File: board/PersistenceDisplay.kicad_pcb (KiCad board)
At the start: 2 copper layers, 100 x 100 mm, 574 parts, among them J1 Conn_01x01, J2 Conn_01x01, J3 Conn_01x04, J4 Conn_01x04, J5 Conn_01x01, J6 Conn_01x01, J7 Conn_01x02, J8 Conn_01x01, J9 Conn_01x01, Q1 2N7002, Q10 2N7002, Q11 2N7002, Q12 2N7002, Q13 2N7002, Q14 2N7002, Q15 2N7002, Q16 2N7002, Q17 2N7002, Q18 2N7002, Q19 2N7002, Q2 2N7002, Q20 2N7002, Q21 2N7002, Q22 2N7002, Q23 2N7002, Q24 2N7002, Q25 2N7002, Q26 2N7002, Q27 2N7002, Q28 2N7002, Q29 2N7002, Q3 2N7002, Q30 2N7002, Q31 2N7002, Q32 2N7002, Q33 2N7002, Q34 2N7002, Q35 2N7002, Q36 2N7002, Q37 2N7002, Q38 2N7002, Q39 2N7002, Q4 2N7002, Q40 2N7002, Q41 SS8550, Q42 SS8550, Q43 SS8550, Q44 SS8550, Q45 SS8550, Q46 SS8550, Q47 SS8550, Q48 SS8550, Q49 SS8550, Q5 2N7002, Q50 SS8550, Q51 SS8550, Q52 SS8550, Q53 SS8550, Q54 SS8550, Q55 SS8550, Q56 SS8550, Q57 SS8550, Q58 SS8550, Q59 SS8550, Q6 2N7002, Q60 SS8550, Q7 2N7002, Q8 2N7002, Q9 2N7002, U1 AMS1117-3V3, U2 STM32F103VETx, U3 nrf24l01, U4 LM393, Y1 8 MHz, Y2 32.768 kHz, Y3 16 MHz

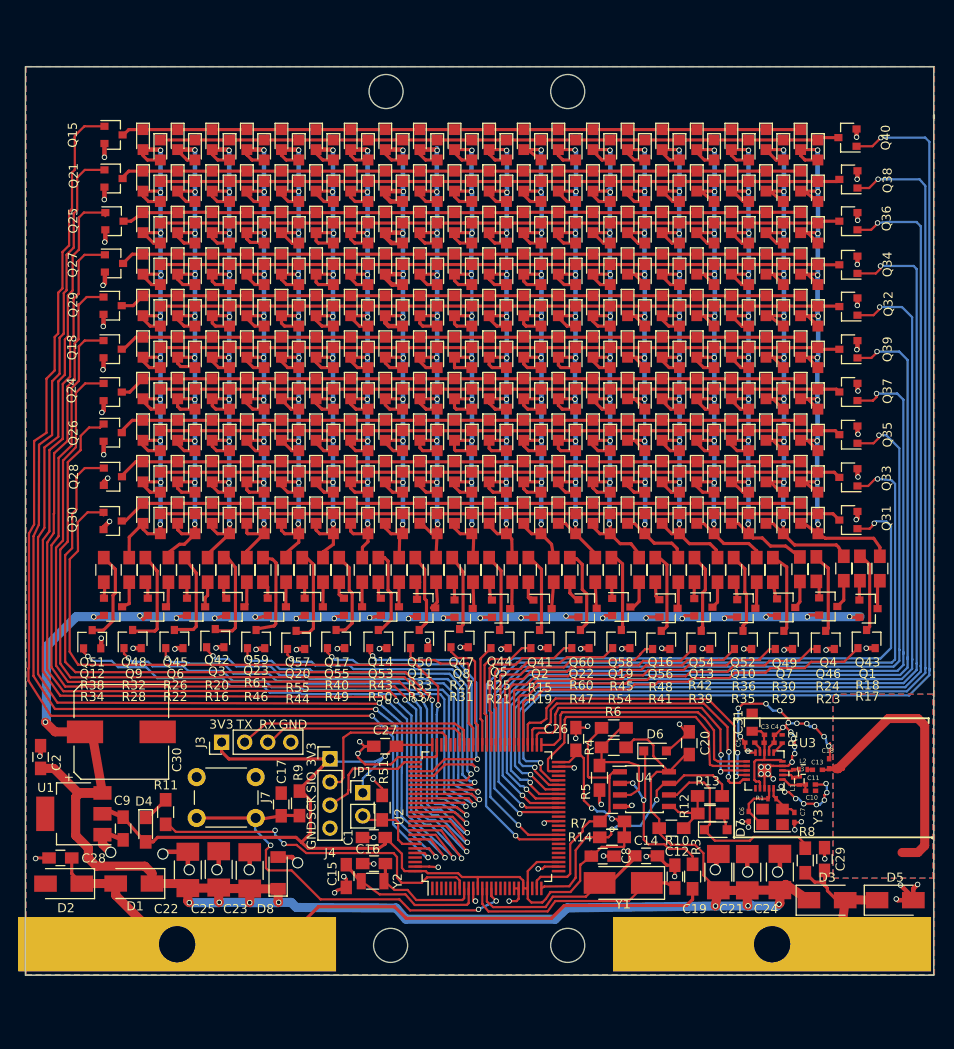
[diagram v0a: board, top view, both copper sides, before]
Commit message: Moved around components and added cutouts
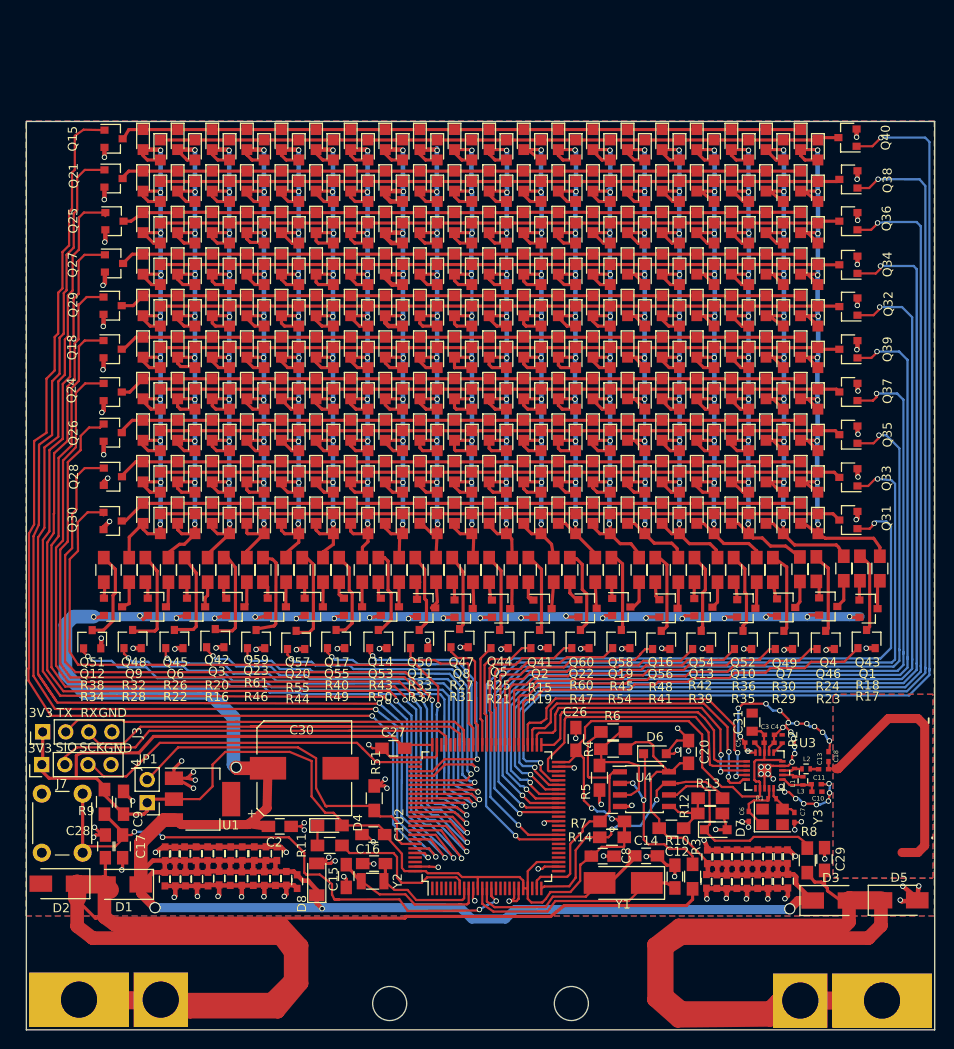
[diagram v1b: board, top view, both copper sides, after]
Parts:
- added C32: 22 uF, Capacitors_SMD:C_0603, F.Cu at (69.1, 136.9)
- added C33: 22 uF, Capacitors_SMD:C_0603, F.Cu at (70.4, 136.9)
- added C34: 22 uF, Capacitors_SMD:C_0603, F.Cu at (72.9, 136.9)
- added C35: 22 uF, Capacitors_SMD:C_0603, F.Cu at (71.6, 136.9)
- added C36: 22 uF, Capacitors_SMD:C_0603, F.Cu at (67.9, 139.7)
- added C37: 22 uF, Capacitors_SMD:C_0603, F.Cu at (71.6, 139.6)
- added C38: 22 uF, Capacitors_SMD:C_0603, F.Cu at (78.0, 136.9)
- added C39: 22 uF, Capacitors_SMD:C_0603, F.Cu at (72.8, 139.6)
- added C40: 22 uF, Capacitors_SMD:C_0603, F.Cu at (66.8, 139.7)
- added C41: 22 uF, Capacitors_SMD:C_0603, F.Cu at (65.6, 139.7)
- added C42: 22 uF, Capacitors_SMD:C_0603, F.Cu at (69.2, 139.7)
- added C43: 22 uF, Capacitors_SMD:C_0603, F.Cu at (75.4, 139.6)
- added C44: 22 uF, Capacitors_SMD:C_0603, F.Cu at (74.1, 139.6)
- added C45: 22 uF, Capacitors_SMD:C_0603, F.Cu at (70.4, 139.7)
- added C46: 22 uF, Capacitors_SMD:C_0603, F.Cu at (77.8, 139.6)
- added C47: 22 uF, Capacitors_SMD:C_0603, F.Cu at (130.9, 137.2)
- added C48: 22 uF, Capacitors_SMD:C_0603, F.Cu at (128.7, 137.2)
- added C49: 22 uF, Capacitors_SMD:C_0603, F.Cu at (129.8, 137.2)
- added C50: 22 uF, Capacitors_SMD:C_0603, F.Cu at (127.5, 137.2)
- added C51: 22 uF, Capacitors_SMD:C_0603, F.Cu at (79.0, 139.6)
- added C52: 22 uF, Capacitors_SMD:C_0603, F.Cu at (80.2, 140.0)
- added C53: 22 uF, Capacitors_SMD:C_0603, F.Cu at (76.6, 139.6)
- added C54: 22 uF, Capacitors_SMD:C_0603, F.Cu at (126.5, 137.3)
- added C55: 22 uF, Capacitors_SMD:C_0603, F.Cu at (125.4, 137.3)
- added C56: 22 uF, Capacitors_SMD:C_0603, F.Cu at (132.1, 137.2)
- added C57: 22 uF, Capacitors_SMD:C_0603, F.Cu at (134.2, 137.2)
- added C58: 22 uF, Capacitors_SMD:C_0603, F.Cu at (128.6, 140.0)
- added C59: 22 uF, Capacitors_SMD:C_0603, F.Cu at (127.5, 140.0)
- added C60: 22 uF, Capacitors_SMD:C_0603, F.Cu at (129.7, 140.0)
- added C61: 22 uF, Capacitors_SMD:C_0603, F.Cu at (134.2, 139.9)
- added C62: 22 uF, Capacitors_SMD:C_0603, F.Cu at (130.9, 140.0)
- added C63: 22 uF, Capacitors_SMD:C_0603, F.Cu at (132.1, 140.0)
- added C64: 22 uF, Capacitors_SMD:C_0603, F.Cu at (133.1, 137.2)
- added C65: 22 uF, Capacitors_SMD:C_0603, F.Cu at (133.1, 140.0)
- added C66: 22 uF, Capacitors_SMD:C_0603, F.Cu at (126.4, 140.0)
- added C67: 22 uF, Capacitors_SMD:C_0603, F.Cu at (125.3, 140.0)
- added J10: Conn_01x01, PersistenceDisplay:BigSlot, F.Cu at (147.0, 148.0)
- added J11: Conn_01x01, PersistenceDisplay:ContactPad, F.Cu at (56.2, 153.1)
- added J12: Conn_01x01, PersistenceDisplay:ContactPad, F.Cu at (144.6, 153.2)
- added J13: Conn_01x01, PersistenceDisplay:BigSlot, F.Cu at (66.0, 148.0)
- added J14: Conn_01x01, PersistenceDisplay:BigSlot, F.Cu at (72.0, 148.0)
- added J15: Conn_01x01, PersistenceDisplay:BigSlot, F.Cu at (141.0, 148.0)
- added J16: Conn_01x01, PersistenceDisplay:BigSlot, F.Cu at (135.0, 148.0)
- added J17: Conn_01x01, PersistenceDisplay:BigSlot, F.Cu at (129.0, 148.0)
- C19, C21, C22, C23, C24, C25: value 100 uF -> 22 uF; footprint Capacitors_SMD:C_1210_HandSoldering -> Capacitors_SMD:C_0603
- moved J1 110.3 mm to (54.0, 148.0)
- moved J2 99.6 mm to (60.0, 148.0)
- moved C24 56.6 mm to (76.8, 136.9)
- moved C21 54.3 mm to (75.5, 136.9)
- moved C19 52.4 mm to (74.2, 136.9)
- moved J4 31.7 mm to (52.1, 127.1), turned to 90 degrees
- moved C2 27.4 mm to (78.3, 133.9), turned to 180 degrees
- moved JP1 23.8 mm to (63.7, 131.3), turned to 180 degrees
- moved R9 21.5 mm to (59.0, 131.2)
- moved C30 20.5 mm to (81.0, 127.5)
- moved D4 20.3 mm to (83.8, 133.8), turned to 0 degrees
- moved J3 19.7 mm to (52.2, 123.5)
- moved J7 19.2 mm to (56.6, 130.3), turned to 270 degrees
- moved R11 18.4 mm to (83.8, 136.0), turned to 180 degrees
- moved C17 18.1 mm to (61.0, 136.1), turned to 270 degrees
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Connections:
- C3 pad 2: Net-(C3-Pad2) -> +3V3
- C31 pad 2: Net-(C3-Pad2) -> +3V3
- C4 pad 2: Net-(C3-Pad2) -> +3V3
- U3 pad 15: Net-(C3-Pad2) -> +3V3
- U3 pad 18: Net-(C3-Pad2) -> +3V3
- U3 pad 7: Net-(C3-Pad2) -> +3V3
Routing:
- net Net-(C29-Pad2): track 15.7 -> 120.3 mm
- net Net-(C28-Pad2): track 89.0 -> 188.4 mm
- net +5V: track 307.9 -> 377.8 mm, vias 28 -> 24
- net +3V3: track 136.1 -> 200.4 mm, vias 3 -> 2
- net GND: track 179.0 -> 235.0 mm, vias 110 -> 127
- net PA10: track 23.2 -> 54.7 mm
- net Net-(JP1-Pad2): track 8.14 -> 38.8 mm
- net PA13: track 18.8 -> 45.4 mm
- net PA14: track 13.0 -> 39.0 mm
- net PC13: track 38.5 -> 17.3 mm, vias 2 -> 0
- net PA9: track 26.8 -> 46.7 mm
- net NRST: track 47.1 -> 64.3 mm, vias 3 -> 4
- net Net-(C3-Pad2): track 11.3 -> 0.00 mm
- net PB7: track 119.7 -> 123.3 mm
- net Net-(C13-Pad1): track 0.58 -> 1.89 mm
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
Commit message: Moved the brushes to the other side of the board
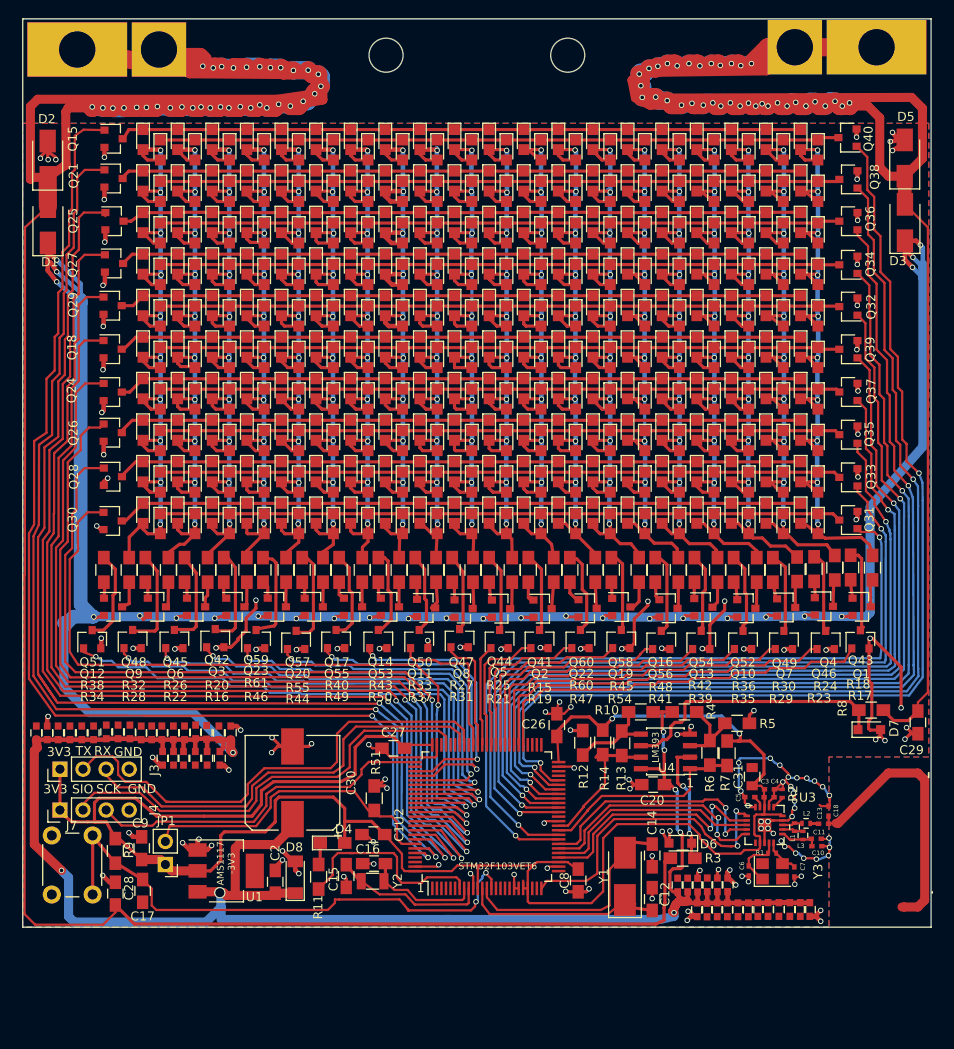
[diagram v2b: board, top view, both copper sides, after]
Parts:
- moved J12 105.0 mm to (144.0, 48.2)
- moved J6 105.0 mm to (135.0, 48.2)
- moved J11 104.6 mm to (56.0, 48.5)
- moved J5 104.6 mm to (65.0, 48.5)
- moved J8 104.4 mm to (110.0, 49.0)
- moved J9 104.4 mm to (90.0, 49.0)
- moved J10 95.8 mm to (146.8, 52.2)
- moved J15 95.8 mm to (140.8, 52.2)
- moved J16 95.8 mm to (134.8, 52.2)
- moved J17 95.8 mm to (128.8, 52.2)
- moved J1 95.5 mm to (53.1, 52.5)
- moved J13 95.5 mm to (65.2, 52.5)
- moved J14 95.5 mm to (71.2, 52.5)
- moved J2 95.5 mm to (59.1, 52.5)
- moved D5 81.7 mm to (147.1, 60.3), turned to 90 degrees
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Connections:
- R13 pad 2: PA2 -> PB1
- R14 pad 1: PA2 -> PB1
- R6 pad 2: PA1 -> PB0
- R7 pad 1: PA1 -> PB0
- U2 pad 24: PA1 -> (no net)
- U2 pad 29: (no net) -> PA4
- U2 pad 30: (no net) -> PA5
- U2 pad 31: (no net) -> PA6
- U2 pad 32: (no net) -> PA7
- U2 pad 35: (no net) -> PB0
- U2 pad 36: (no net) -> PB1
- U2 pad 48: PB11 -> (no net)
- U2 pad 51: PB12 -> (no net)
- U2 pad 52: PB13 -> (no net)
- U2 pad 53: PB14 -> (no net)
- U2 pad 54: PB15 -> (no net)
- U3 pad 1: PB12 -> PA2
- U3 pad 2: PB11 -> PA4
- U3 pad 3: PB13 -> PA5
- U3 pad 4: PB15 -> PA7
- U3 pad 5: PB14 -> PA6
- U4 pad 1: PA1 -> PB0
- U4 pad 7: PA2 -> PB1
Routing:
- net Net-(C28-Pad2): track 188.4 -> 345.2 mm, vias 0 -> 34
- net Net-(C29-Pad2): track 120.3 -> 242.6 mm, vias 0 -> 36
- net +5V: track 377.8 -> 465.8 mm, vias 24 -> 34
- net PB15: track 35.1 -> 0.00 mm, vias 2 -> 0
- net PB14: track 34.6 -> 0.00 mm, vias 2 -> 0
- net PB13: track 32.4 -> 0.00 mm, vias 2 -> 0
- net PB11: track 32.0 -> 0.00 mm
- net PB12: track 29.8 -> 0.00 mm
- net PA1: track 27.5 -> 0.00 mm
- net PA4: track 0.00 -> 27.4 mm, vias 0 -> 2
- net PA7: track 0.00 -> 27.2 mm, vias 0 -> 2
- net PA6: track 0.00 -> 26.7 mm, vias 0 -> 2
- net PA5: track 0.00 -> 24.4 mm
- net PB0: track 0.00 -> 23.1 mm
- net +3V3: track 200.4 -> 221.7 mm
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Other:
- board text added: "1"
- board text added: "AMS1117 -3V3"
- board text added: "LM393"
- board text added: "PERSISTENCE DISPLAY BY DANIEL MARKS CC-BY-SA 4.0"
- board text added: "STM32F103VET6"

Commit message: JLCPCB order 2020-05-20
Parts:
- moved J17 2.26 mm to (128.9, 54.5)
- moved J16 2.21 mm to (134.9, 54.5)
- moved J15 2.10 mm to (140.8, 54.4)
- moved J10 2.10 mm to (146.8, 54.4)
- moved J13 2.02 mm to (64.9, 54.5)
- moved J2 2.00 mm to (59.0, 54.5)
- moved J14 2.00 mm to (71.2, 54.5)
- moved J1 1.95 mm to (53.0, 54.5)
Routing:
- net Net-(C28-Pad2): track 345.2 -> 220.6 mm, vias 34 -> 0
- net Net-(C29-Pad2): track 242.6 -> 132.4 mm, vias 36 -> 0
- net GND: track 236.2 -> 240.1 mm
- net Net-(C13-Pad2): track 30.5 -> 29.1 mm
- added copper zone on F.Cu, net Net-(C28-Pad2)
- added copper zone on F.Cu, net Net-(C29-Pad2)

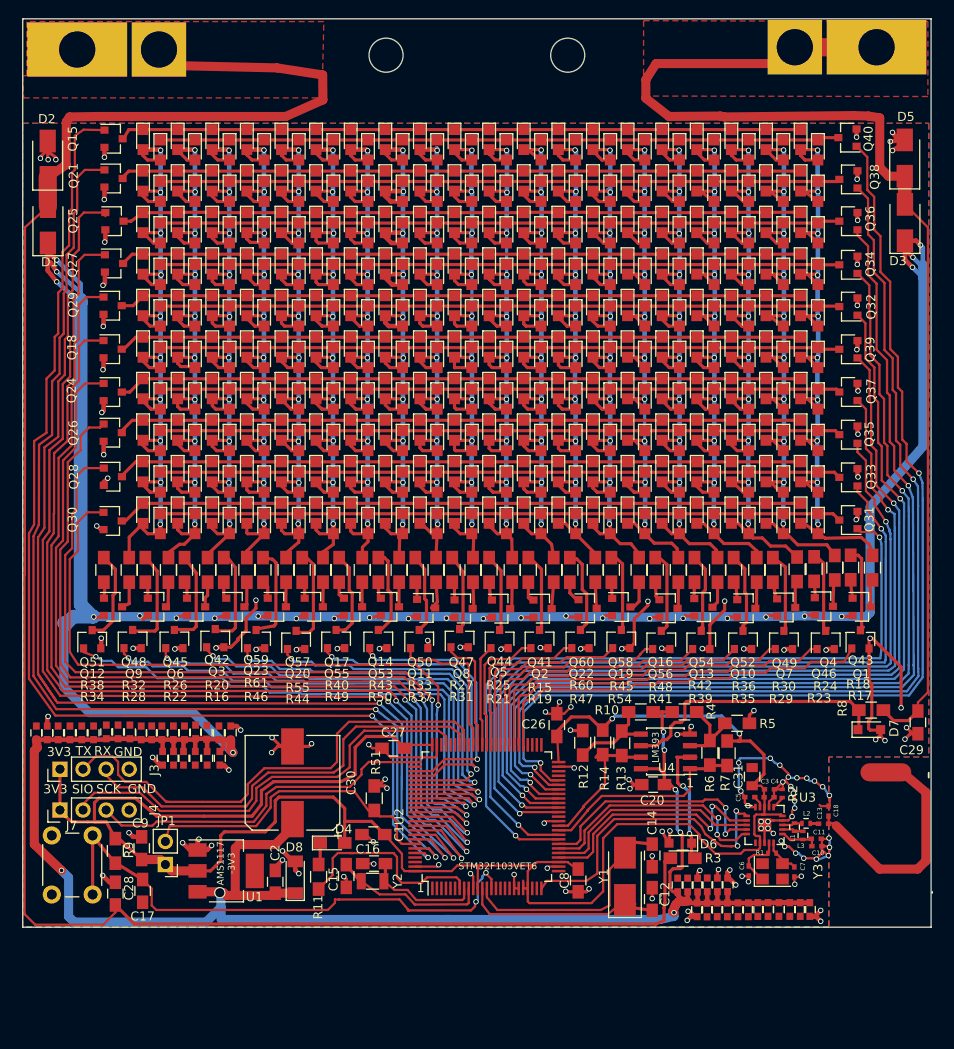
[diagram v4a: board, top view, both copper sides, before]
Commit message: Changed to using hall effect sensors
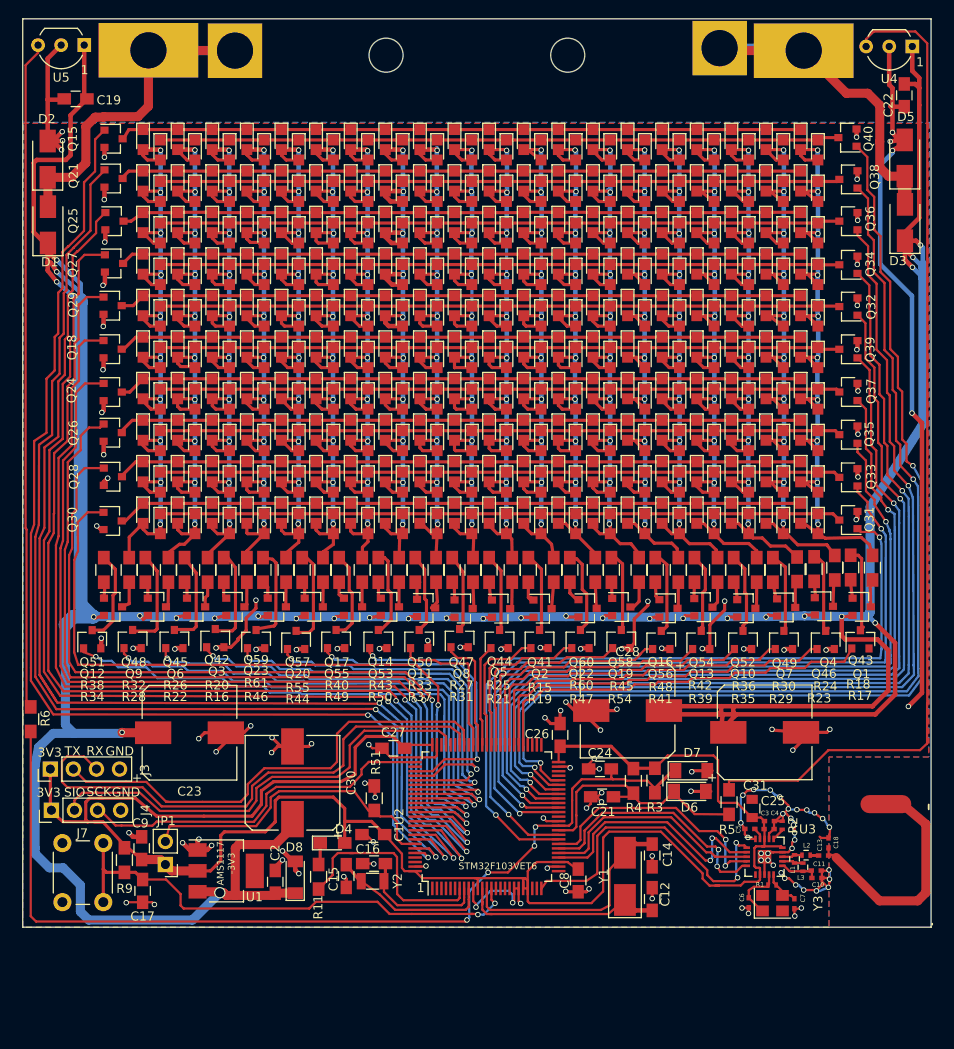
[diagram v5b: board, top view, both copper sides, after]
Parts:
- removed C20: 0.1 uF, Capacitors_SMD:C_0805_HandSoldering
- removed C29: 1 nF, Capacitors_SMD:C_0805_HandSoldering
- removed C32, C33, C34, C35, C36, C37, C38, C39, C40, C41, C42, C43, C44, C45, C46, C47, C48, C49, C50, C51, C52, C53, C54, C55, C56, C57, C58, C59, C60, C61, C62, C63, C64, C65, C66, C67: 22 uF, Capacitors_SMD:C_0603
- removed J1, J10, J13, J14, J15, J16, J17, J2: Conn_01x01, PersistenceDisplay:BigSlot
- removed R10, R12, R14, R7: 10k, Resistors_SMD:R_0805_HandSoldering
- removed R13: 47k, Resistors_SMD:R_0805_HandSoldering
- removed R8: 100k, Resistors_SMD:R_0805_HandSoldering
- added U5: OH137, TO_SOT_Packages_THT:TO-92_Inline_Wide, F.Cu at (56.8, 47.9)
- C19, C22: value 22 uF -> 0.1 uF; footprint Capacitors_SMD:C_0603 -> Capacitors_SMD:C_0805_HandSoldering
- C21, C24: value 22 uF -> 22 pF; footprint Capacitors_SMD:C_0603 -> Capacitors_SMD:C_0805_HandSoldering
- C23, C25: value 22 uF -> 1000 uF; footprint Capacitors_SMD:C_0603 -> Capacitors_SMD:CP_Elec_10x10.5
- C28: value 1 nF -> 1000 uF; footprint Capacitors_SMD:C_0805_HandSoldering -> Capacitors_SMD:CP_Elec_10x10.5
- D1, D2, D3, D5: value M7 -> SS34
- D6, D7: value 1N4148WS -> 3.3V; footprint Diodes_SMD:D_SOD-323_HandSoldering -> Diodes_SMD:D_MiniMELF
- R3: value 100k -> 1k
- R4: value 10k -> 1k
- R5: value 10k -> 150R
- R6: value 47k -> 150R
- U4: value LM393 -> OH137; footprint Housings_SOIC:SOIC-8_3.9x4.9mm_Pitch1.27mm -> TO_SOT_Packages_THT:TO-92_Inline_Wide
- moved C22 102.1 mm to (147.1, 53.4)
- moved U4 82.2 mm to (147.9, 48.0)
- moved R6 74.9 mm to (50.9, 122.1)
- moved C19 69.8 mm to (55.8, 53.8), turned to 0 degrees
- moved C24 61.0 mm to (113.5, 127.6), turned to 0 degrees
- moved C21 60.3 mm to (113.8, 130.6), turned to 0 degrees
- moved C25 60.0 mm to (131.7, 123.5), turned to 0 degrees
- moved C28 59.9 mm to (116.6, 121.2), turned to 180 degrees
- moved D7 20.1 mm to (123.6, 127.8)
- moved R4 9.44 mm to (117.2, 128.9), turned to 90 degrees
- moved R3 9.08 mm to (119.6, 128.8), turned to 90 degrees
- moved R5 8.73 mm to (127.8, 131.2), turned to 270 degrees
- moved J5 8.37 mm to (73.4, 48.6)
- moved J6 8.28 mm to (126.7, 48.4)
- moved J12 8.03 mm to (136.0, 48.6)
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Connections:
- C19 pad 1: +5V -> GND
- C19 pad 2: GND -> +5V
- C21 pad 1: +5V -> GND
- C21 pad 2: GND -> PB0
- C22 pad 1: +5V -> GND
- C22 pad 2: GND -> +5V
- C24 pad 1: +5V -> GND
- C24 pad 2: GND -> PB1
- C28 pad 1: GND -> +5V
- C28 pad 2: Net-(C28-Pad2) -> GND
- D1 pad 2: Net-(C28-Pad2) -> Net-(D1-Pad2)
- D2 pad 1: Net-(C28-Pad2) -> Net-(D1-Pad2)
- D6 pad 1: Net-(D6-Pad1) -> PB0
- D7 pad 1: Net-(D7-Pad1) -> PB1
- J11 pad 1: Net-(C28-Pad2) -> Net-(D1-Pad2)
- J5 pad 1: Net-(C28-Pad2) -> Net-(D1-Pad2)
- R3 pad 1: Net-(C28-Pad2) -> PB1
- R3 pad 2: Net-(D6-Pad1) -> +3V3
- R4 pad 1: Net-(R4-Pad1) -> PB0
- R4 pad 2: +5V -> +3V3
- R5 pad 1: GND -> Net-(R5-Pad1)
- R5 pad 2: Net-(R4-Pad1) -> PB0
- R6 pad 1: Net-(R4-Pad1) -> Net-(R6-Pad1)
- R6 pad 2: PB0 -> PB1
- U4 pad 1: PB0 -> +5V
- U4 pad 2: Net-(D6-Pad1) -> GND
- U4 pad 3: Net-(R4-Pad1) -> Net-(R5-Pad1)
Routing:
- net Net-(C28-Pad2): track 220.6 -> 0.00 mm
- net Net-(R5-Pad1): track 0.00 -> 110.0 mm
- net PB1: track 16.4 -> 106.5 mm, vias 0 -> 4
- net Net-(D3-Pad2): track 132.4 -> 43.5 mm
- net GND: track 240.1 -> 322.7 mm, vias 138 -> 132
- net Net-(R6-Pad1): track 0.00 -> 73.6 mm
- net Net-(D1-Pad2): track 0.00 -> 47.8 mm
- net Net-(D7-Pad1): track 30.2 -> 0.00 mm
- net Net-(D6-Pad1): track 14.3 -> 0.00 mm, vias 2 -> 0
- net PA10: track 49.2 -> 60.9 mm
- net Net-(R10-Pad1): track 10.7 -> 0.00 mm
- net Net-(R4-Pad1): track 8.77 -> 0.00 mm
- net +5V: track 465.8 -> 457.5 mm, vias 34 -> 29
- net PB0: track 23.1 -> 29.5 mm
- net NRST: track 61.0 -> 56.6 mm
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- removed copper zone on F.Cu, net Net-(C28-Pad2)
- removed copper zone on F.Cu, net Net-(D3-Pad2)
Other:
- board text removed: "LM393"
